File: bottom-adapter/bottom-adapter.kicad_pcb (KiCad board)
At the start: 2 copper layers, 97 x 97 mm, 26 parts, among them J1 Solar Cell, J2 Burn Wire

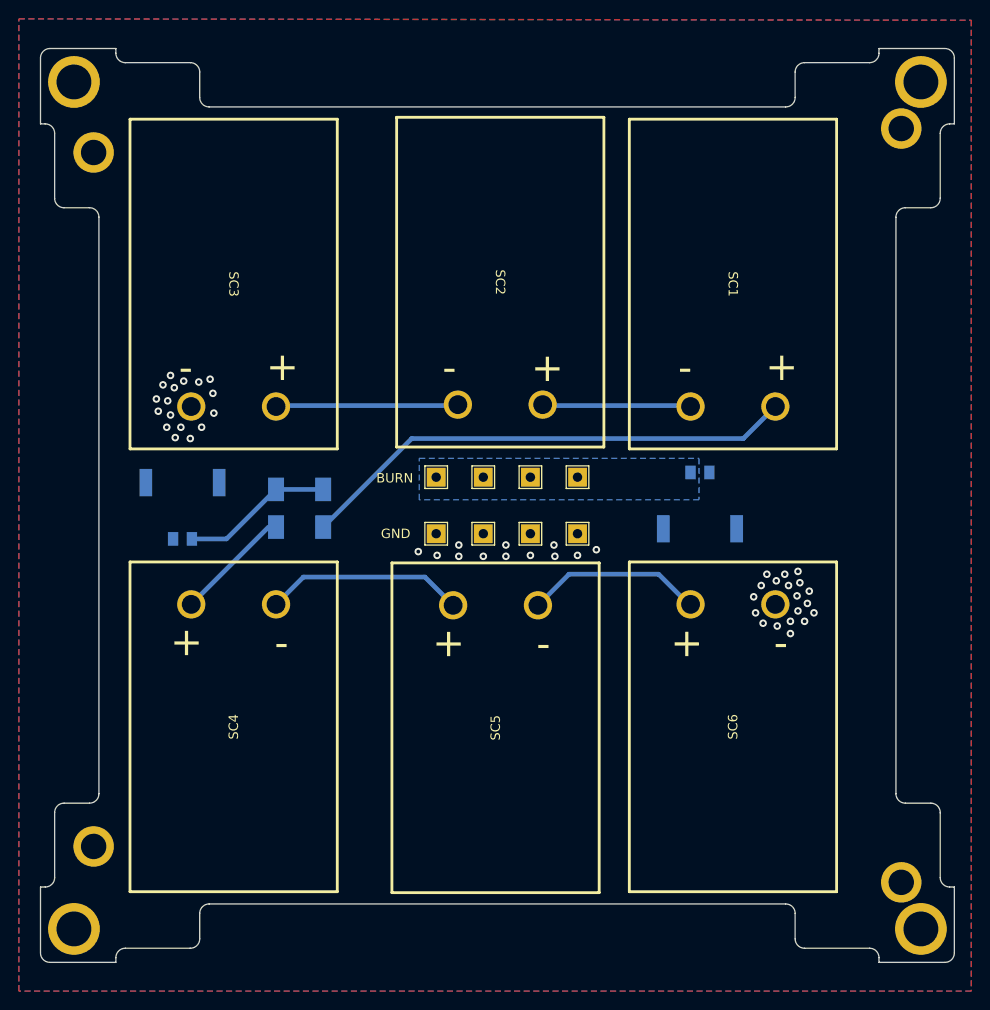
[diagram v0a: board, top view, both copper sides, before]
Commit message: removed solar panels from bottom adapter and moved burn connector
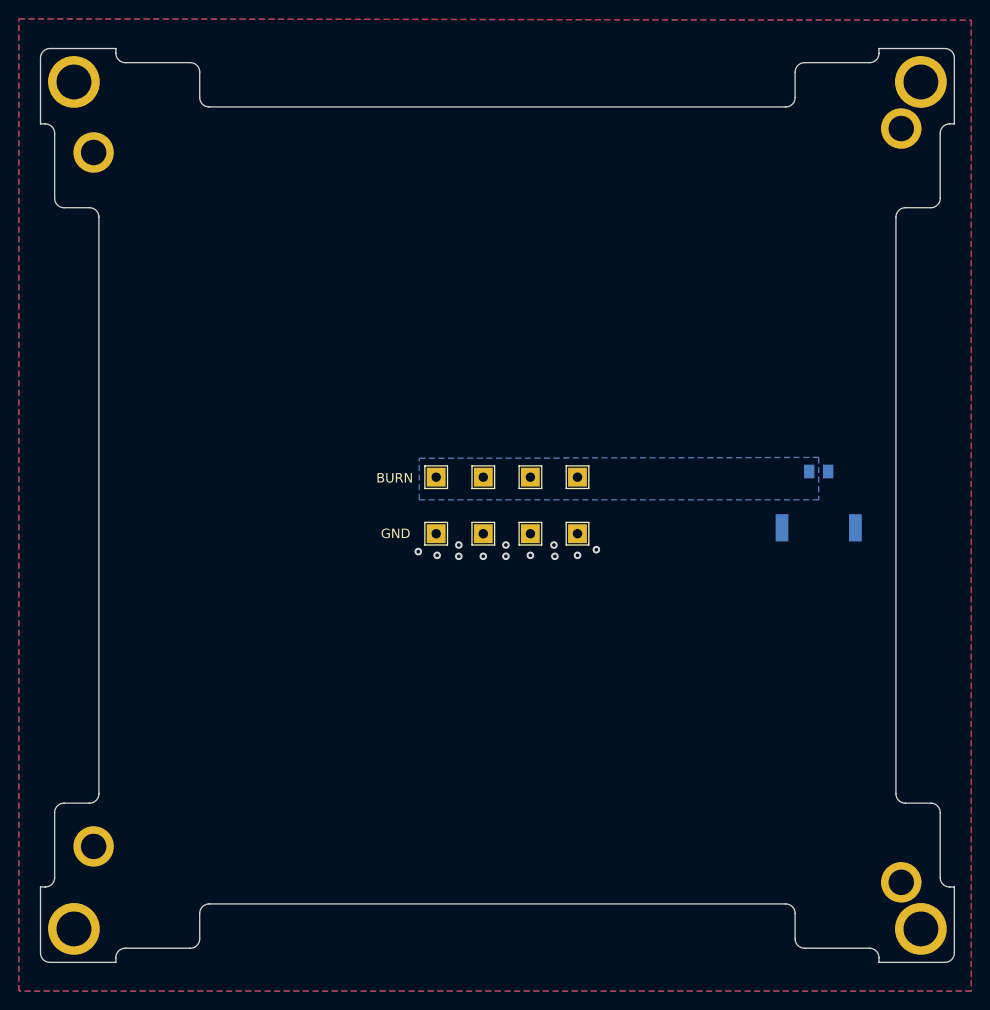
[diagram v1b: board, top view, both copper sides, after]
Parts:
- removed D1, D2: CDBA240LL-HF, ISP:DO-214AC
- removed J1: Solar Cell, ISP:pico_lock_2mm_2circuit
- removed SC1, SC2, SC3, SC4, SC5, SC6: SM101K07TF, ISP:SM101K07TF
- moved J2 12.6 mm to (153.6, 94.9)
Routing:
- net Net-(D1-Pad2): track 53.3 -> 0.00 mm
- net Net-(SC4-Pad2): track 21.2 -> 0.00 mm
- net Net-(SC2-Pad2): track 19.4 -> 0.00 mm
- net Net-(SC5-Pad2): track 19.0 -> 0.00 mm
- net VSOLAR: track 16.1 -> 0.00 mm
- net Net-(SC1-Pad2): track 15.9 -> 0.00 mm
- net Net-(D2-Pad2): track 12.4 -> 0.00 mm
- net GND: vias 48 -> 12
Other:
- board text removed: "+"
- board text removed: "-"

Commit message: added updated bottom adapter w/ silkscreen
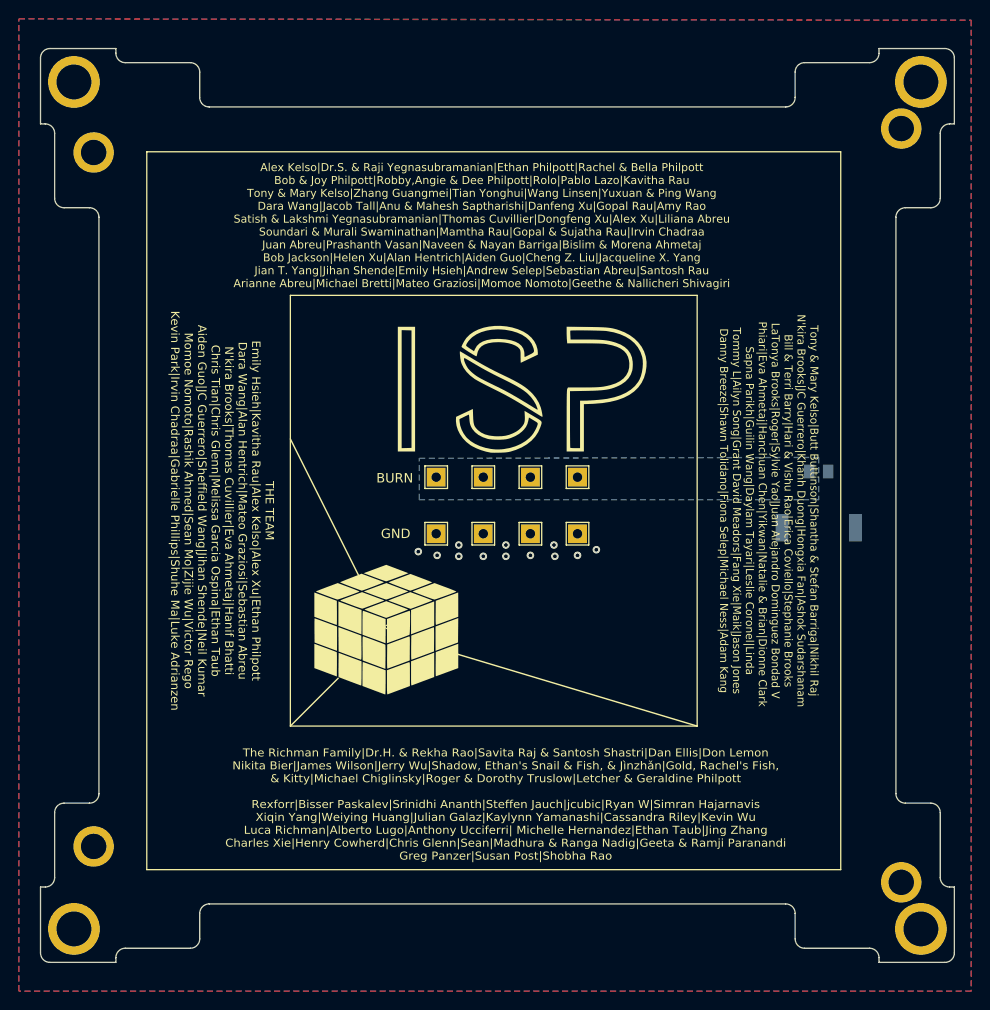
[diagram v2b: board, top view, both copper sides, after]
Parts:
- added G: LOGO, LOGO, F.Cu at (119.4, 86.4)
- added G***: LOGO, LOGO, F.Cu at (106.7, 111.8)
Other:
- board text added: "Alex Kelso|Dr.S. & Raji Yegnasubramanian|Ethan Philpott|Rachel & Bella Philpott Bob & Joy Philpott|Robby,Angie & Dee Philpott|Rolo|Pablo Lazo|Kavitha Rau Tony & Mary Kelso|Zhang Guangmei|Tian Yonghui|Wang Linsen|Yuxuan & Ping Wang Dara Wang|Jacob Tall|Anu & Mahesh Saptharishi|Danfeng Xu|Gopal Rau|Amy Rao Satish & Lakshmi Yegnasubramanian|Thomas Cuvillier|Dongfeng Xu|Alex Xu|Liliana Abreu Soundari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"
- board text added: "THE TEAM Emily Hsieh|Kavitha Rau|Alex Kelso|Alex Xu|Ethan Philpott Dara Wang|Alan Hentrich|Mateo Graziosi|Sebastian Abreu N'kira Brooks|Thomas Cuvillier|Eva Ahmetaj|Hanif Bhatti Chris Tian|Chris Glenn|Melissa Garcia Ospina|Ethan Taub Aiden Guo|JC Guerrero|Sheffield Wang|Jihan Shende|Neil Kumar Momoe Nomoto|Rashik Ahmed|Sean Mo|Zijie Wu|Victor Rego Kevin Park|Irvin Chadraa|Gabrielle Phillips|Shuhe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"
- board text added: "The Richman Family|Dr.H. & Rekha Rao|Savita Raj & Santosh Shastri|Dan Ellis|Don Lemon Nikita Bier|James Wilson|Jerry Wu|Shadow, Ethan's Snail & Fish, & Jìnzhǎn|Gold, Rachel's Fish, & Kitty|Michael Chiglinsky|Roger & Dorothy Truslow|Letcher & Geraldine Philpott Rexforr|Bisser Paskalev|Srinidhi Ananth|Steffen Jauch|jcubic|Ryan W|Simran Hajarnavis Xiqin Yang|Weiying Huang|Julian Galaz|Kaylynn Yamana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"
- board text added: "Tony & Mary Kelso|Butt Buttinson|Shantha & Stefan Barriga|Nikhil Raj N'kira Brooks|JC Guerrero|Khanh Duong|Hongxia Fan|Ashok Sudarshanam Bill & Terri Barry|Hari & Vishu Rao|Erica Coviello|Stephanie Brooks LaTonya Brooks|Roger|Sylvie Yao|Juan Alejandro Dominguez Bondad V Phiari|Eva Ahmetaj|Hanchuan Chen|Yikwan|Natalie & Brian|Dionne Clark Sapna Parikh|Guilin Wang|Daylam Tayari|Leslie Coronel|Linda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"

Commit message: fixed zoning and burn pads
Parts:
- removed Burn2, Burn4: Burn, TestPoint:TestPoint_THTPad_2.0x2.0mm_Drill1.0mm
- removed GND3, GND4: GND, TestPoint:TestPoint_THTPad_2.0x2.0mm_Drill1.0mm
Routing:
- net GND: vias 12 -> 9

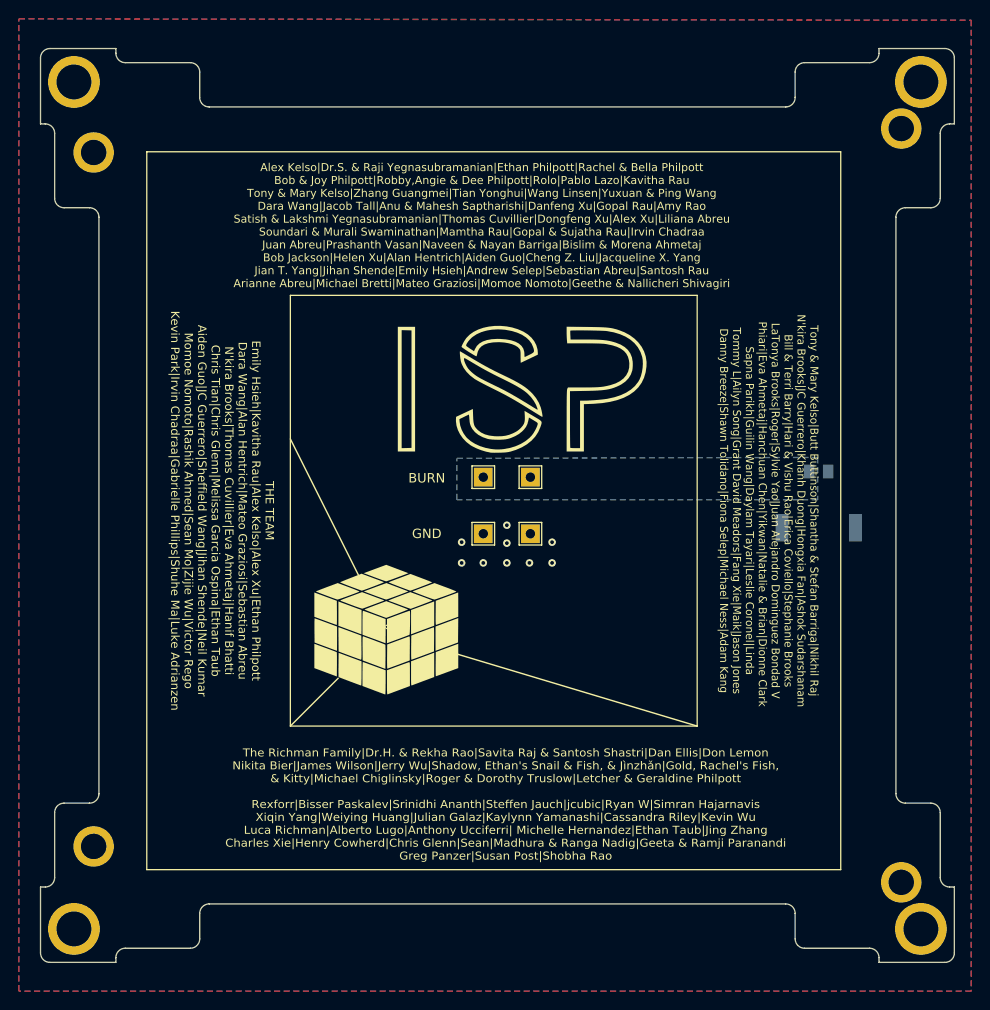
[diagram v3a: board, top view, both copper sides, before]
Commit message: new batt board and bottom adapter w/ fixed silkscreen
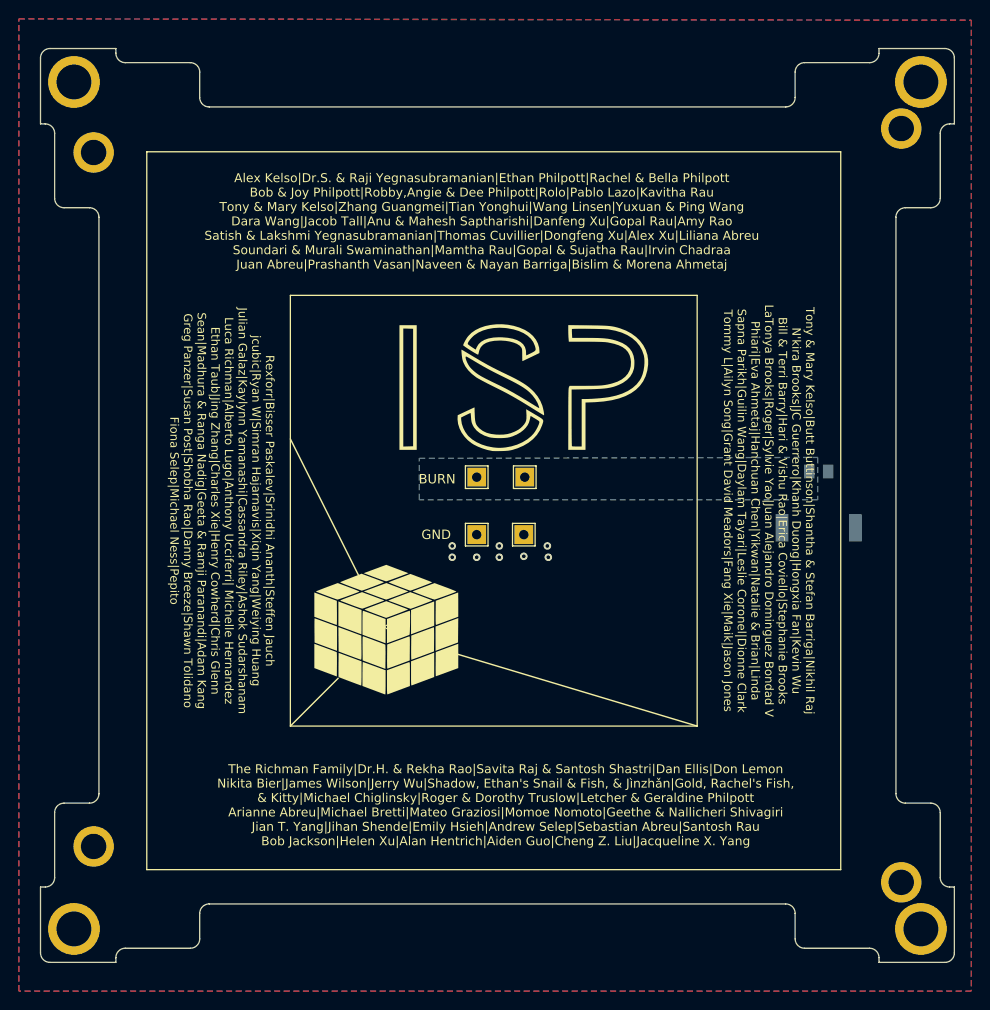
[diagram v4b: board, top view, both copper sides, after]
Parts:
- removed Burn3: Burn, TestPoint:TestPoint_THTPad_2.0x2.0mm_Drill1.0mm
- added Burn2: Burn, TestPoint:TestPoint_THTPad_2.0x2.0mm_Drill1.0mm, F.Cu at (121.4, 95.5)
- moved GND1 0.71 mm to (121.3, 101.6)
- moved GND2 0.71 mm to (116.3, 101.6)
- moved Burn1 0.70 mm to (116.3, 95.5)
- moved G 0.24 mm to (119.6, 86.2)
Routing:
- net GND: vias 9 -> 8
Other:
- board text added: "Rexforr|Bisser Paskalev|Srinidhi Ananth|Steffen Jauch jcubic|Ryan W|Simran Hajarnavis|Xiqin Yang|Weiying Huang Julian Galaz|Kaylynn Yamanashi|Cassandra Riley|Ashok Sudarshanam Luca Richman|Alberto Lugo|Anthony Ucciferri| Michelle Hernandez Ethan Taub|Jing Zhang|Charles Xie|Henry Cowherd|Chris Glenn Sean|Madhura & Ranga Nadig|Geeta & Ramji Paranandi|Adam Kang Greg Panzer|Susan Post|Shobha Rao|Dann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"
- board text added: "The Richman Family|Dr.H. & Rekha Rao|Savita Raj & Santosh Shastri|Dan Ellis|Don Lemon Nikita Bier|James Wilson|Jerry Wu|Shadow, Ethan's Snail & Fish, & Jìnzhǎn|Gold, Rachel's Fish, & Kitty|Michael Chiglinsky|Roger & Dorothy Truslow|Letcher & Geraldine Philpott Arianne Abreu|Michael Bretti|Mateo Graziosi|Momoe Nomoto|Geethe & Nallicheri Shivagiri Jian T. Yang|Jihan Shende|Emily Hsieh|Andrew Selep|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"
- board text added: "Tony & Mary Kelso|Butt Buttinson|Shantha & Stefan Barriga|Nikhil Raj N'kira Brooks|JC Guerrero|Khanh Duong|Hongxia Fan|Kevin Wu Bill & Terri Barry|Hari & Vishu Rao|Erica Coviello|Stephanie Brooks LaTonya Brooks|Roger|Sylvie Yao|Juan Alejandro Dominguez Bondad V Phiari|Eva Ahmetaj|Hanchuan Chen|Yikwan|Natalie & Brian|Linda Sapna Parikh|Guilin Wang|Daylam Tayari|Leslie Coronel|Dionne Clark Tommy L|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"
- board text removed: "THE TEAM Emily Hsieh|Kavitha Rau|Alex Kelso|Alex Xu|Ethan Philpott Dara Wang|Alan Hentrich|Mateo Graziosi|Sebastian Abreu N'kira Brooks|Thomas Cuvillier|Eva Ahmetaj|Hanif Bhatti Chris Tian|Chris Glenn|Melissa Garcia Ospina|Ethan Taub Aiden Guo|JC Guerrero|Sheffield Wang|Jihan Shende|Neil Kumar Momoe Nomoto|Rashik Ahmed|Sean Mo|Zijie Wu|Victor Rego Kevin Park|Irvin Chadraa|Gabrielle Phillips|Shuhe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"
- board text removed: "The Richman Family|Dr.H. & Rekha Rao|Savita Raj & Santosh Shastri|Dan Ellis|Don Lemon Nikita Bier|James Wilson|Jerry Wu|Shadow, Ethan's Snail & Fish, & Jìnzhǎn|Gold, Rachel's Fish, & Kitty|Michael Chiglinsky|Roger & Dorothy Truslow|Letcher & Geraldine Philpott Rexforr|Bisser Paskalev|Srinidhi Ananth|Steffen Jauch|jcubic|Ryan W|Simran Hajarnavis Xiqin Yang|Weiying Huang|Julian Galaz|Kaylynn Yamana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"
- board text removed: "Tony & Mary Kelso|Butt Buttinson|Shantha & Stefan Barriga|Nikhil Raj N'kira Brooks|JC Guerrero|Khanh Duong|Hongxia Fan|Ashok Sudarshanam Bill & Terri Barry|Hari & Vishu Rao|Erica Coviello|Stephanie Brooks LaTonya Brooks|Roger|Sylvie Yao|Juan Alejandro Dominguez Bondad V Phiari|Eva Ahmetaj|Hanchuan Chen|Yikwan|Natalie & Brian|Dionne Clark Sapna Parikh|Guilin Wang|Daylam Tayari|Leslie Coronel|Linda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"
